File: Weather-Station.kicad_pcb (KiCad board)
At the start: 2 copper layers, 177.8 x 106.7 mm, 3 parts, among them J1 Conn_01x22, J2 Conn_01x22, U1 ESP32-S3-DevKitC

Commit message: WIP: Finding pin headers/rows
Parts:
- added J3: Conn_02x19_Odd_Even, Connector_PinHeader_2.54mm:PinHeader_2x19_P2.54mm_Vertical, F.Cu at (83.1, 60.3)
- added J4: Conn_02x19_Odd_Even, Connector_PinHeader_2.54mm:PinHeader_2x19_P2.54mm_Vertical, F.Cu at (144.1, 60.3)
- moved J1 56.9 mm to (218.9, 52.0)
- moved U1 56.9 mm to (218.9, 52.0)
- moved J2 56.9 mm to (241.8, 52.0)

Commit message: WIP: Adding display and ESP32
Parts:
- moved J3 118.1 mm to (185.3, 119.4)
- moved J4 118.1 mm to (246.3, 119.4)
- moved J2 95.0 mm to (314.8, 112.7)
- moved J1 95.0 mm to (291.9, 112.7)
- moved U1 95.0 mm to (291.9, 112.7)
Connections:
- U1 pad 1: Net-(U1-3V3-Pad1) -> unconnected-(U1-3V3-Pad1)
- U1 pad 2: Net-(U1-3V3-Pad1) -> unconnected-(U1-3V3-Pad2)
- U1 pad 22: Net-(U1-GND-Pad22) -> unconnected-(U1-GND-Pad22)
- U1 pad 23: Net-(U1-GND-Pad22) -> unconnected-(U1-GND-Pad23)
- U1 pad 24: Net-(U1-GND-Pad22) -> unconnected-(U1-U0TXD/GPIO43-Pad24)
- U1 pad 44: Net-(U1-GND-Pad22) -> unconnected-(U1-GND-Pad44)

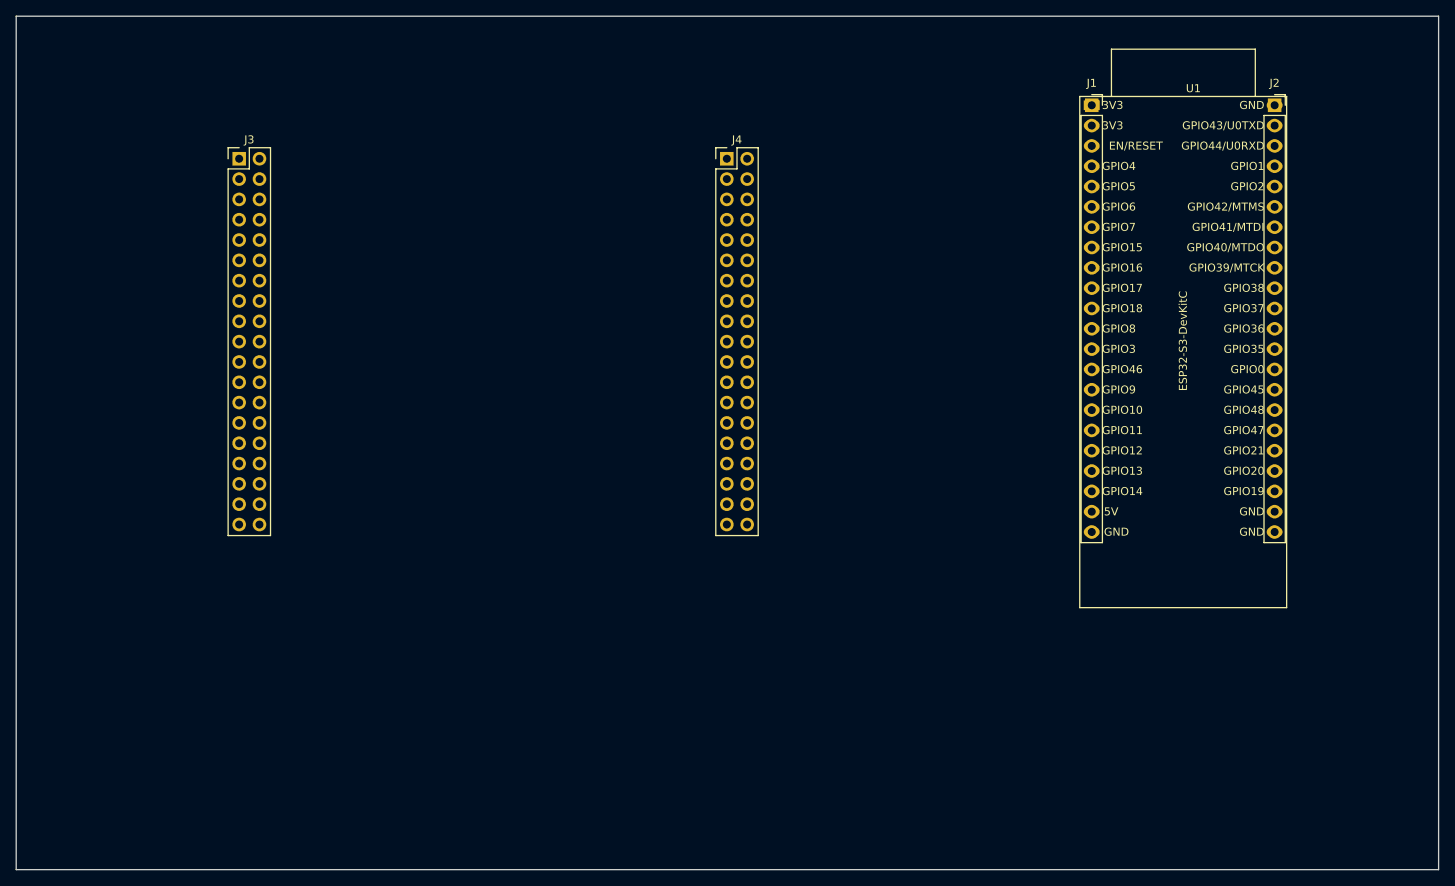
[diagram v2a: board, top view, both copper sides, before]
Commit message: WIP: Finding components on jlcpcb and merging
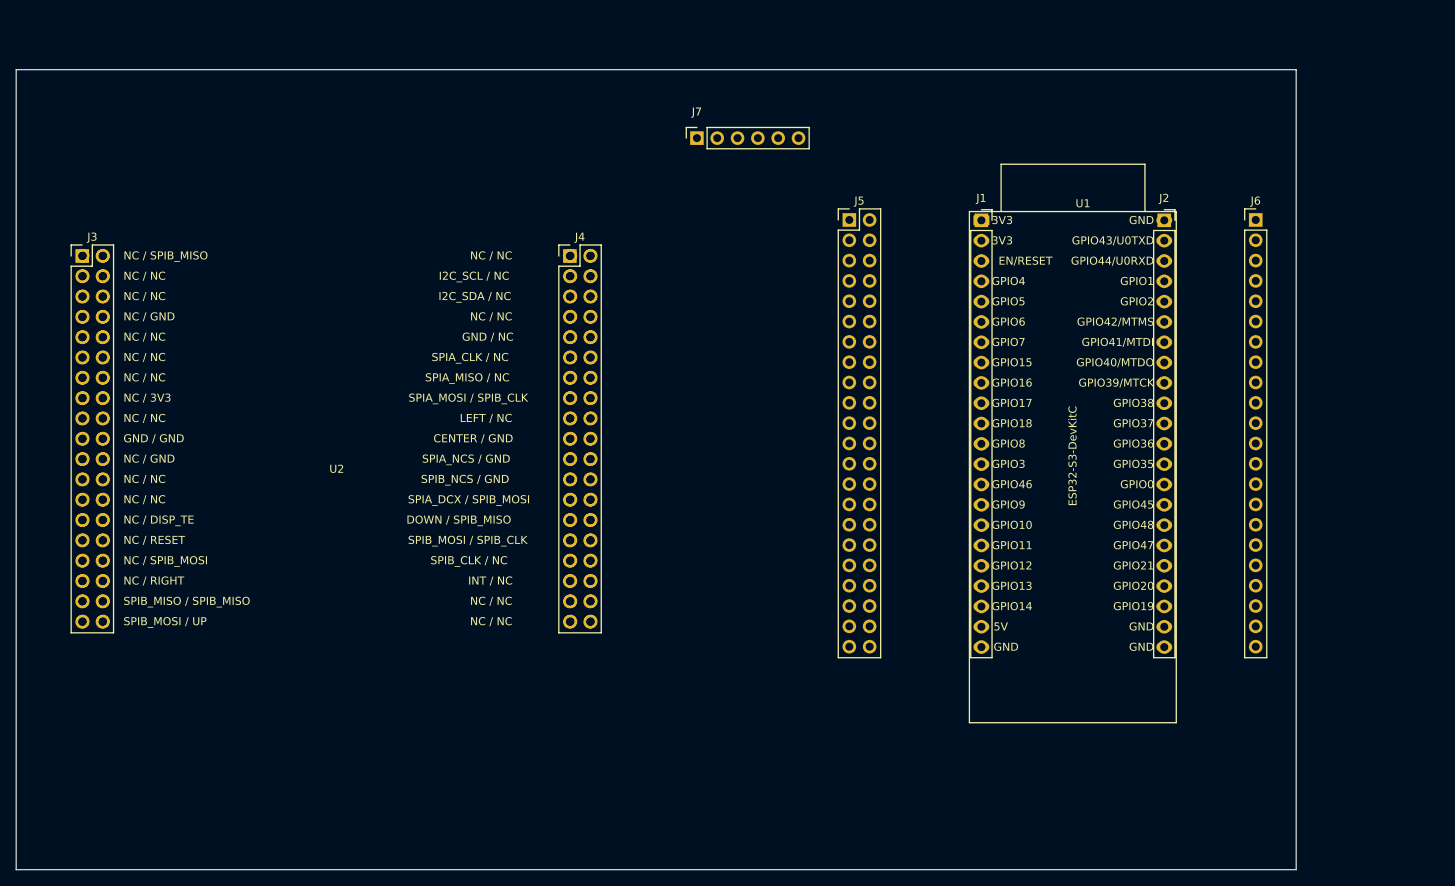
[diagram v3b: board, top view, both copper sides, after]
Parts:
- added J5: Conn_02x22_Odd_Even, Connector_PinHeader_2.54mm:PinHeader_2x22_P2.54mm_Vertical, F.Cu at (261.6, 127.1)
- added J6: Conn_01x22, Connector_PinHeader_2.54mm:PinHeader_1x22_P2.54mm_Vertical, F.Cu at (312.4, 127.1)
- added J7: Conn_01x06, Connector_PinSocket_2.54mm:PinSocket_1x06_P2.54mm_Vertical, F.Cu at (242.6, 116.8)
- added U2: X-NUCLEO-GFX01M2, custom:ST_NUCLEO-GFX01M2, F.Cu at (165.8, 131.5)
- J3: value Conn_02x19_Odd_Even -> CN2
- J4: value Conn_02x19_Odd_Even -> CN3
- moved J3 23.1 mm to (165.7, 131.6)
- moved J4 23.1 mm to (226.7, 131.6)
- moved J1 19.9 mm to (278.1, 127.1)
- moved J2 19.9 mm to (301.0, 127.1)
- moved U1 19.9 mm to (278.1, 127.1)
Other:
- board size 177.8 x 106.7 mm -> 160 x 100 mm

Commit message: WIP: Started routing
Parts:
- moved J3 3.74 mm to (169.5, 131.4)
- moved J4 3.74 mm to (230.4, 131.4)
- moved U2 3.67 mm to (169.5, 131.4)
- moved J5 2.54 mm to (264.2, 127.1)
- moved J1 0.07 mm to (278.1, 127.0)
- moved J2 0.07 mm to (301.0, 127.0)
- moved U1 0.07 mm to (278.1, 127.0)
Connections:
- J1 pad 1: unconnected-(J1-Pin_1-Pad1) -> Net-(J1-Pin_1)
- J1 pad 10: unconnected-(J1-Pin_10-Pad10) -> Net-(J1-Pin_10)
- J1 pad 11: unconnected-(J1-Pin_11-Pad11) -> Net-(J1-Pin_11)
- J1 pad 12: unconnected-(J1-Pin_12-Pad12) -> Net-(J1-Pin_12)
- J1 pad 13: unconnected-(J1-Pin_13-Pad13) -> Net-(J1-Pin_13)
- J1 pad 14: unconnected-(J1-Pin_14-Pad14) -> Net-(J1-Pin_14)
- J1 pad 15: unconnected-(J1-Pin_15-Pad15) -> Net-(J1-Pin_15)
- J1 pad 16: unconnected-(J1-Pin_16-Pad16) -> Net-(J1-Pin_16)
- J1 pad 17: unconnected-(J1-Pin_17-Pad17) -> Net-(J1-Pin_17)
- J1 pad 18: unconnected-(J1-Pin_18-Pad18) -> Net-(J1-Pin_18)
- J1 pad 19: unconnected-(J1-Pin_19-Pad19) -> Net-(J1-Pin_19)
- J1 pad 2: unconnected-(J1-Pin_2-Pad2) -> Net-(J1-Pin_2)
- J1 pad 20: unconnected-(J1-Pin_20-Pad20) -> Net-(J1-Pin_20)
- J1 pad 21: unconnected-(J1-Pin_21-Pad21) -> Net-(J1-Pin_21)
- J1 pad 22: unconnected-(J1-Pin_22-Pad22) -> Net-(J1-Pin_22)
- J1 pad 3: unconnected-(J1-Pin_3-Pad3) -> Net-(J1-Pin_3)
- J1 pad 4: unconnected-(J1-Pin_4-Pad4) -> Net-(J1-Pin_4)
- J1 pad 5: unconnected-(J1-Pin_5-Pad5) -> Net-(J1-Pin_5)
- J1 pad 6: unconnected-(J1-Pin_6-Pad6) -> Net-(J1-Pin_6)
- J1 pad 7: unconnected-(J1-Pin_7-Pad7) -> Net-(J1-Pin_7)
- J1 pad 8: unconnected-(J1-Pin_8-Pad8) -> Net-(J1-Pin_8)
- J1 pad 9: unconnected-(J1-Pin_9-Pad9) -> Net-(J1-Pin_9)
- J2 pad 1: unconnected-(J2-Pin_1-Pad1) -> Net-(J2-Pin_1)
- J2 pad 10: unconnected-(J2-Pin_10-Pad10) -> Net-(J2-Pin_10)
- J2 pad 11: unconnected-(J2-Pin_11-Pad11) -> Net-(J2-Pin_11)
- J2 pad 12: unconnected-(J2-Pin_12-Pad12) -> Net-(J2-Pin_12)
- J2 pad 13: unconnected-(J2-Pin_13-Pad13) -> Net-(J2-Pin_13)
- J2 pad 14: unconnected-(J2-Pin_14-Pad14) -> Net-(J2-Pin_14)
- J2 pad 15: unconnected-(J2-Pin_15-Pad15) -> Net-(J2-Pin_15)
- J2 pad 16: unconnected-(J2-Pin_16-Pad16) -> Net-(J2-Pin_16)
- J2 pad 17: unconnected-(J2-Pin_17-Pad17) -> Net-(J2-Pin_17)
- J2 pad 18: unconnected-(J2-Pin_18-Pad18) -> Net-(J2-Pin_18)
- J2 pad 19: unconnected-(J2-Pin_19-Pad19) -> Net-(J2-Pin_19)
- J2 pad 2: unconnected-(J2-Pin_2-Pad2) -> Net-(J2-Pin_2)
- J2 pad 20: unconnected-(J2-Pin_20-Pad20) -> Net-(J2-Pin_20)
- J2 pad 21: unconnected-(J2-Pin_21-Pad21) -> Net-(J2-Pin_21)
- J2 pad 22: unconnected-(J2-Pin_22-Pad22) -> Net-(J2-Pin_22)
- J2 pad 3: unconnected-(J2-Pin_3-Pad3) -> Net-(J2-Pin_3)
- J2 pad 4: unconnected-(J2-Pin_4-Pad4) -> Net-(J2-Pin_4)
- J2 pad 5: unconnected-(J2-Pin_5-Pad5) -> Net-(J2-Pin_5)
- J2 pad 6: unconnected-(J2-Pin_6-Pad6) -> Net-(J2-Pin_6)
- J2 pad 7: unconnected-(J2-Pin_7-Pad7) -> Net-(J2-Pin_7)
- J2 pad 8: unconnected-(J2-Pin_8-Pad8) -> Net-(J2-Pin_8)
- J2 pad 9: unconnected-(J2-Pin_9-Pad9) -> Net-(J2-Pin_9)
- J3 pad 16: unconnected-(J3-Pin_16-Pad16) -> Net-(J3-Pin_16)
- J5 pad 1: unconnected-(J5-Pin_1-Pad1) -> Net-(J3-Pin_16)
- J5 pad 10: unconnected-(J5-Pin_10-Pad10) -> Net-(J1-Pin_5)
- J5 pad 12: unconnected-(J5-Pin_12-Pad12) -> Net-(J1-Pin_6)
- J5 pad 14: unconnected-(J5-Pin_14-Pad14) -> Net-(J1-Pin_7)
- J5 pad 16: unconnected-(J5-Pin_16-Pad16) -> Net-(J1-Pin_8)
- J5 pad 18: unconnected-(J5-Pin_18-Pad18) -> Net-(J1-Pin_9)
- J5 pad 2: unconnected-(J5-Pin_2-Pad2) -> Net-(J1-Pin_1)
- J5 pad 20: unconnected-(J5-Pin_20-Pad20) -> Net-(J1-Pin_10)
- J5 pad 22: unconnected-(J5-Pin_22-Pad22) -> Net-(J1-Pin_11)
- J5 pad 24: unconnected-(J5-Pin_24-Pad24) -> Net-(J1-Pin_12)
- J5 pad 26: unconnected-(J5-Pin_26-Pad26) -> Net-(J1-Pin_13)
- J5 pad 28: unconnected-(J5-Pin_28-Pad28) -> Net-(J1-Pin_14)
- J5 pad 30: unconnected-(J5-Pin_30-Pad30) -> Net-(J1-Pin_15)
- J5 pad 32: unconnected-(J5-Pin_32-Pad32) -> Net-(J1-Pin_16)
- J5 pad 34: unconnected-(J5-Pin_34-Pad34) -> Net-(J1-Pin_17)
- J5 pad 36: unconnected-(J5-Pin_36-Pad36) -> Net-(J1-Pin_18)
- J5 pad 38: unconnected-(J5-Pin_38-Pad38) -> Net-(J1-Pin_19)
- J5 pad 4: unconnected-(J5-Pin_4-Pad4) -> Net-(J1-Pin_2)
- J5 pad 40: unconnected-(J5-Pin_40-Pad40) -> Net-(J1-Pin_20)
- J5 pad 42: unconnected-(J5-Pin_42-Pad42) -> Net-(J1-Pin_21)
- J5 pad 44: unconnected-(J5-Pin_44-Pad44) -> Net-(J1-Pin_22)
- J5 pad 6: unconnected-(J5-Pin_6-Pad6) -> Net-(J1-Pin_3)
- J5 pad 8: unconnected-(J5-Pin_8-Pad8) -> Net-(J1-Pin_4)
- J6 pad 1: unconnected-(J6-Pin_1-Pad1) -> Net-(J2-Pin_1)
- J6 pad 10: unconnected-(J6-Pin_10-Pad10) -> Net-(J2-Pin_10)
- J6 pad 11: unconnected-(J6-Pin_11-Pad11) -> Net-(J2-Pin_11)
- J6 pad 12: unconnected-(J6-Pin_12-Pad12) -> Net-(J2-Pin_12)
- J6 pad 13: unconnected-(J6-Pin_13-Pad13) -> Net-(J2-Pin_13)
- J6 pad 14: unconnected-(J6-Pin_14-Pad14) -> Net-(J2-Pin_14)
- J6 pad 15: unconnected-(J6-Pin_15-Pad15) -> Net-(J2-Pin_15)
- J6 pad 16: unconnected-(J6-Pin_16-Pad16) -> Net-(J2-Pin_16)
- J6 pad 17: unconnected-(J6-Pin_17-Pad17) -> Net-(J2-Pin_17)
- J6 pad 18: unconnected-(J6-Pin_18-Pad18) -> Net-(J2-Pin_18)
- J6 pad 19: unconnected-(J6-Pin_19-Pad19) -> Net-(J2-Pin_19)
- J6 pad 2: unconnected-(J6-Pin_2-Pad2) -> Net-(J2-Pin_2)
- J6 pad 20: unconnected-(J6-Pin_20-Pad20) -> Net-(J2-Pin_20)
- J6 pad 21: unconnected-(J6-Pin_21-Pad21) -> Net-(J2-Pin_21)
- J6 pad 22: unconnected-(J6-Pin_22-Pad22) -> Net-(J2-Pin_22)
- J6 pad 3: unconnected-(J6-Pin_3-Pad3) -> Net-(J2-Pin_3)
- J6 pad 4: unconnected-(J6-Pin_4-Pad4) -> Net-(J2-Pin_4)
- J6 pad 5: unconnected-(J6-Pin_5-Pad5) -> Net-(J2-Pin_5)
- J6 pad 6: unconnected-(J6-Pin_6-Pad6) -> Net-(J2-Pin_6)
- J6 pad 7: unconnected-(J6-Pin_7-Pad7) -> Net-(J2-Pin_7)
- J6 pad 8: unconnected-(J6-Pin_8-Pad8) -> Net-(J2-Pin_8)
- J6 pad 9: unconnected-(J6-Pin_9-Pad9) -> Net-(J2-Pin_9)
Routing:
- net Net-(J3-Pin_16): track 0.00 -> 101.4 mm
- net Net-(J2-Pin_6): track 0.00 -> 11.4 mm
- net Net-(J2-Pin_3): track 0.00 -> 11.4 mm
- net Net-(J2-Pin_21): track 0.00 -> 11.4 mm
- net Net-(J2-Pin_20): track 0.00 -> 11.4 mm
- net Net-(J2-Pin_2): track 0.00 -> 11.4 mm
- net Net-(J2-Pin_17): track 0.00 -> 11.4 mm
- net Net-(J2-Pin_14): track 0.00 -> 11.4 mm
- net Net-(J2-Pin_13): track 0.00 -> 11.4 mm
- net Net-(J2-Pin_10): track 0.00 -> 11.4 mm
- net Net-(J1-Pin_6): track 0.00 -> 11.4 mm
- net Net-(J1-Pin_3): track 0.00 -> 11.4 mm
- net Net-(J1-Pin_21): track 0.00 -> 11.4 mm
- net Net-(J1-Pin_20): track 0.00 -> 11.4 mm
- net Net-(J1-Pin_2): track 0.00 -> 11.4 mm
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
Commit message: WIP: Routing started
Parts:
- moved J1 48.3 mm to (278.1, 78.7)
- moved J2 48.3 mm to (301.0, 78.7)
- moved U1 48.3 mm to (278.1, 78.7)
- moved J5 48.3 mm to (264.2, 78.8)
- moved J6 48.3 mm to (312.4, 78.8)
- moved J7 43.2 mm to (240.9, 73.7)
- moved J3 17.1 mm to (168.9, 114.3)
- moved J4 17.1 mm to (229.9, 114.3)
- moved U2 17.1 mm to (168.9, 114.3)
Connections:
- J2 pad 1: Net-(J2-Pin_1) -> GND
- J2 pad 21: Net-(J2-Pin_21) -> GND
- J2 pad 22: Net-(J2-Pin_22) -> GND
- J3 pad 16: Net-(J3-Pin_16) -> unconnected-(J3-Pin_16-Pad16)
- J3 pad 30: unconnected-(J3-Pin_30-Pad30) -> /DISP_RESET
- J3 pad 34: unconnected-(J3-Pin_34-Pad34) -> /RIGHT
- J3 pad 38: unconnected-(J3-Pin_38-Pad38) -> /UP
- J4 pad 11: unconnected-(J4-Pin_11-Pad11) -> /DISP_SCLK
- J4 pad 15: unconnected-(J4-Pin_15-Pad15) -> /DISP_MOSI
- J4 pad 17: unconnected-(J4-Pin_17-Pad17) -> /LEFT
- J4 pad 19: unconnected-(J4-Pin_19-Pad19) -> /CENTER
- J4 pad 21: unconnected-(J4-Pin_21-Pad21) -> /DISP_CS
- J4 pad 25: unconnected-(J4-Pin_25-Pad25) -> /DISP_DC
- J4 pad 27: unconnected-(J4-Pin_27-Pad27) -> /DOWN
- J5 pad 1: Net-(J3-Pin_16) -> +3.3V
- J5 pad 13: unconnected-(J5-Pin_13-Pad13) -> /CENTER
- J5 pad 15: unconnected-(J5-Pin_15-Pad15) -> /RIGHT
- J5 pad 17: unconnected-(J5-Pin_17-Pad17) -> /DOWN
- J5 pad 19: unconnected-(J5-Pin_19-Pad19) -> /LEFT
- J5 pad 21: unconnected-(J5-Pin_21-Pad21) -> /UP
- J5 pad 23: unconnected-(J5-Pin_23-Pad23) -> /BME_SDA
- J5 pad 27: unconnected-(J5-Pin_27-Pad27) -> /DISP_DC
- J5 pad 29: unconnected-(J5-Pin_29-Pad29) -> /BME_SCL
- J5 pad 3: unconnected-(J5-Pin_3-Pad3) -> +3.3V
- J5 pad 31: unconnected-(J5-Pin_31-Pad31) -> /DISP_CS
- J5 pad 33: unconnected-(J5-Pin_33-Pad33) -> /DISP_MOSI
- J5 pad 35: unconnected-(J5-Pin_35-Pad35) -> /DISP_SCLK
- J5 pad 39: unconnected-(J5-Pin_39-Pad39) -> /DISP_RESET
- J5 pad 41: unconnected-(J5-Pin_41-Pad41) -> +5V
- J5 pad 43: unconnected-(J5-Pin_43-Pad43) -> GND
- J6 pad 1: Net-(J2-Pin_1) -> GND
- J6 pad 21: Net-(J2-Pin_21) -> GND
- J6 pad 22: Net-(J2-Pin_22) -> GND
- J7 pad 1: unconnected-(J7-Pin_1-Pad1) -> +3.3V
- J7 pad 2: unconnected-(J7-Pin_2-Pad2) -> GND
- J7 pad 3: unconnected-(J7-Pin_3-Pad3) -> /BME_SDA
- J7 pad 4: unconnected-(J7-Pin_4-Pad4) -> /BME_SCL
- J7 pad 5: unconnected-(J7-Pin_5-Pad5) -> GND
- J7 pad 6: unconnected-(J7-Pin_6-Pad6) -> +3.3V
- U1 pad : unconnected-(U1-GND-Pad23) -> (no net)
- U2 pad : unconnected-(U2-NC-Pad38) -> (no net)
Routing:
- net /DISP_RESET: track 0.00 -> 129.7 mm, vias 0 -> 1
- net Net-(J3-Pin_16): track 101.4 -> 0.00 mm
- net /RIGHT: track 0.00 -> 100.0 mm, vias 0 -> 2
- net /CENTER: track 0.00 -> 95.9 mm, vias 0 -> 1
- net /DOWN: track 0.00 -> 94.2 mm
- net /DISP_DC: track 0.00 -> 85.2 mm
- net /LEFT: track 0.00 -> 81.7 mm, vias 0 -> 1
- net /DISP_CS: track 0.00 -> 78.5 mm
- net /BME_SCL: track 0.00 -> 76.0 mm
- net /DISP_MOSI: track 0.00 -> 70.1 mm
- net /DISP_SCLK: track 0.00 -> 62.1 mm
- net /UP: track 0.00 -> 50.2 mm, vias 0 -> 2
- net +3.3V: track 0.00 -> 43.7 mm, vias 0 -> 1
- net /BME_SDA: track 0.00 -> 41.9 mm
- net GND: track 0.00 -> 34.3 mm
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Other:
- board size 160 x 100 mm -> 160 x 140 mm

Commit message: Routing done
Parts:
- removed U1: ESP32-S3-DevKitC, PCM_Espressif:ESP32-S3-DevKitC
- removed U2: X-NUCLEO-GFX01M2, custom:ST_NUCLEO-GFX01M2
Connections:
- J1 pad 22: Net-(J1-Pin_22) -> GND
- J3 pad 16: unconnected-(J3-Pin_16-Pad16) -> +3.3V
- J3 pad 19: unconnected-(J3-Pin_19-Pad19) -> GND
- J3 pad 20: unconnected-(J3-Pin_20-Pad20) -> GND
- J3 pad 22: unconnected-(J3-Pin_22-Pad22) -> GND
- J3 pad 8: unconnected-(J3-Pin_8-Pad8) -> GND
- J4 pad 20: unconnected-(J4-Pin_20-Pad20) -> GND
- J4 pad 9: unconnected-(J4-Pin_9-Pad9) -> GND
- J5 pad 44: Net-(J1-Pin_22) -> GND
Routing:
- net GND: track 34.3 -> 142.1 mm, vias 0 -> 168
- net +3.3V: track 43.7 -> 149.8 mm, vias 1 -> 0
- net /UP: track 50.2 -> 143.5 mm
- net /RIGHT: track 100.0 -> 146.9 mm
- net Net-(J1-Pin_2): track 11.4 -> 22.8 mm
- net Net-(J2-Pin_8): track 11.4 -> 22.9 mm
- net Net-(J2-Pin_3): track 11.4 -> 22.9 mm
- net Net-(J2-Pin_18): track 11.4 -> 22.9 mm
- net Net-(J1-Pin_22): track 11.4 -> 0.00 mm
- net Net-(J2-Pin_9): track 11.4 -> 22.8 mm
- net Net-(J2-Pin_7): track 11.4 -> 22.8 mm
- net Net-(J2-Pin_6): track 11.4 -> 22.8 mm
- net Net-(J2-Pin_4): track 11.4 -> 22.8 mm
- net Net-(J2-Pin_20): track 11.4 -> 22.8 mm
- net Net-(J2-Pin_2): track 11.4 -> 22.8 mm
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- added copper zone on B.Cu, net GND
- added copper zone on F.Cu, net GND
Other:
- board text added: "SCL GPIO"
- board text added: "Weather Station V1.0"
